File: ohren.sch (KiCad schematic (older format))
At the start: 33 parts, among them J1 Conn_01x19_MountingPin, U1 TLC5951RHA, U2 TLC5951RHA

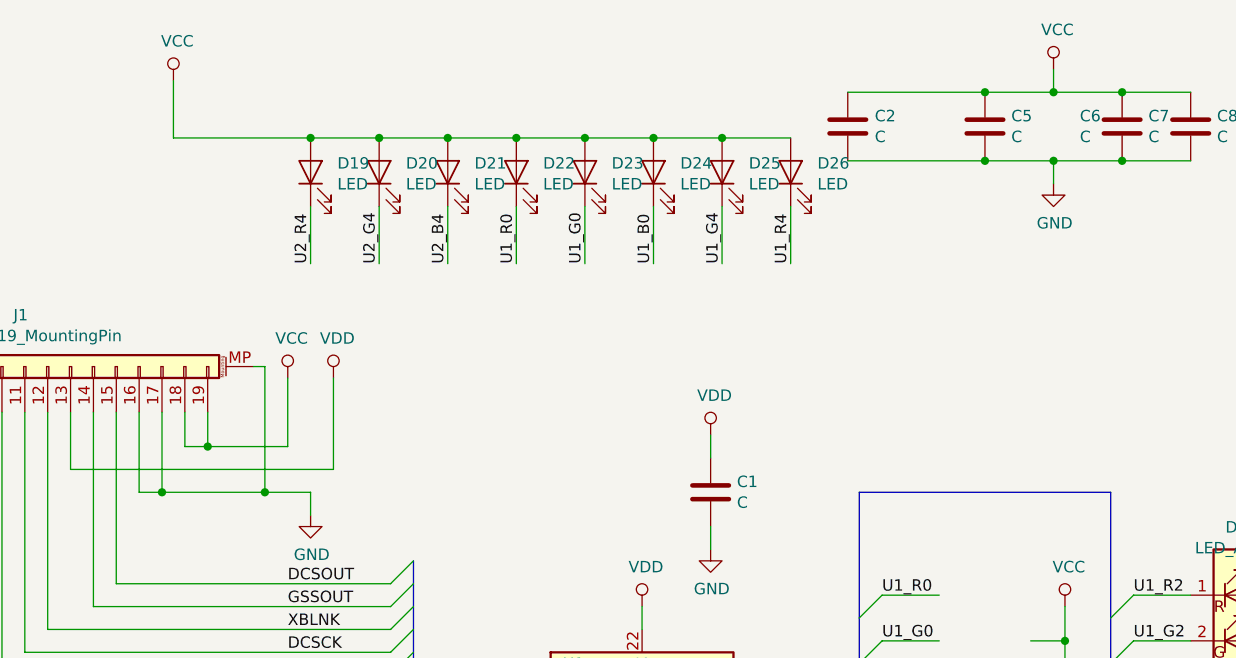
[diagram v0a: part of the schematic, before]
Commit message: Switch to more readily available Molex Easy-On 52746 series FFC
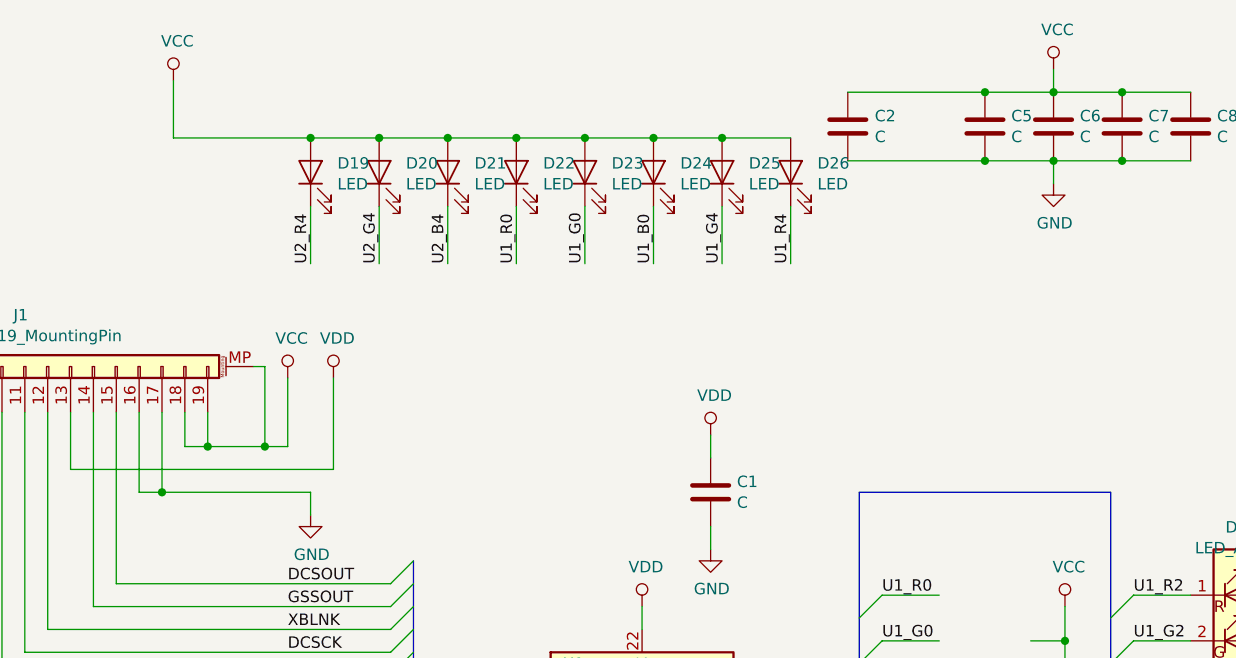
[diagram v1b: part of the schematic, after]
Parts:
- J1: footprint catear-pcb:Molex_Easy-On_54550-1971_1x19_P0.5mm_Horizontal -> catear-pcb:Molex_Easy-On_52746-1971_1x19_P0.5mm_Horizontal
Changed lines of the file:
@@
 Wire Wire Line
 	1900 2850 1900 2750
-Wire Wire Line
-	1900 2750 1700 2750
 Connection ~ 1250 2750
 Wire Wire Line
@@
 F 0 "J1" V 775 2118 50  0000 C CNN
 F 1 "Conn_01x19_MountingPin" V 684 2118 50  0000 C CNN
-F 2 "catear-pcb:Molex_Easy-On_54550-1971_1x19_P0.5mm_Horizontal" H 550 2200 50  0001 C CNN
+F 2 "catear-pcb:Molex_Easy-On_52746-1971_1x19_P0.5mm_Horizontal" H 550 2200 50  0001 C CNN
 F 3 "~" H 550 2200 50  0001 C CNN
 	1    550  2200
@@
 	750  3350 750  2400
 Wire Wire Line
-	1450 2550 1800 2550
+	1450 2550 1700 2550
 Wire Wire Line
 	1650 2200 1700 2200
-Wire Wire Line
-	1700 2200 1700 2750
-Connection ~ 1700 2750
-Wire Wire Line
-	1700 2750 1250 2750
 Wire Wire Line
 	4250 1000 4850 1000
@@
 $Comp
 L Device:C C6
-U 0 0 5D11A988
+U 1 1 5D11A988
 P 5150 1150
 F 0 "C6" H 5265 1196 50  0000 L CNN
@@
 F 2 "Capacitor_SMD:C_1210_3225Metric" H 5188 1000 50  0001 C CNN
 F 3 "~" H 5150 1150 50  0001 C CNN
-	0    5150 1150
+	1    5150 1150
 	1    0    0    -1
 $EndComp
+Wire Wire Line
+	1250 2750 1900 2750
+Wire Wire Line
+	1700 2200 1700 2550
 Wire Bus Line
 	5400 2750 5400 4550
@@
 Wire Bus Line
 	2350 3050 2350 6850
+Connection ~ 1700 2550
+Wire Wire Line
+	1700 2550 1800 2550
 $EndSCHEMATC

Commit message: Design revision D
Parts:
- removed C1: C, Capacitor_SMD:C_0805_2012Metric, symbol Device:C
- removed R1, R2: 2k4, Resistor_SMD:R_0402_1005Metric, symbol Device:R
- removed U1, U2: TLC5951RHA, Package_DFN_QFN:Texas_S-PVQFN-N40_EP4.15x4.15mm_ThermalVias, symbol ohren-rescue:TLC5951RHA-Driver_LED
- added U1: TLC5955RTQ, Package_DFN_QFN:QFN-56-1EP_8x8mm_P0.5mm_EP5.6x5.6mm_ThermalVias, symbol tlc5955:TLC5955RTQ
- C2, C5, C6, C7, C8: footprint Capacitor_SMD:C_1210_3225Metric -> Capacitor_SMD:C_0805_2012Metric
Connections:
- net labels added: GSCLK, LAT, SCLK, SIN, SOUT, U1_B10, U1_B11, U1_B12, U1_B13, U1_B14, U1_B15, U1_B8, U1_B9, U1_G10, U1_G11, U1_G12, U1_G13, U1_G14, U1_G15, U1_G8, U1_G9, U1_R10, U1_R11, U1_R12, U1_R13, U1_R14, U1_R15, U1_R8, U1_R9
- net labels removed: DCSCHAIN, DCSCK, DCSIN, DCSOUT, GSCKB, GSCKG, GSCKR, GSLAT, GSSCHAIN, GSSCK, GSSIN, GSSOUT, U2_B0, U2_B1, U2_B2, U2_B3, U2_B4, U2_B5, U2_B6, U2_B7, U2_G0, U2_G1, U2_G2, U2_G3, U2_G4, U2_G5, U2_G6, U2_G7, U2_R0, U2_R1, U2_R2, U2_R3, U2_R4, U2_R5, U2_R6, U2_R7, XBLNK
- wire segments 245 -> 212
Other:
- moved on the sheet: C2, C3, C5, C6, C7, C8, D10, D11, D12, D13, D14, D15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

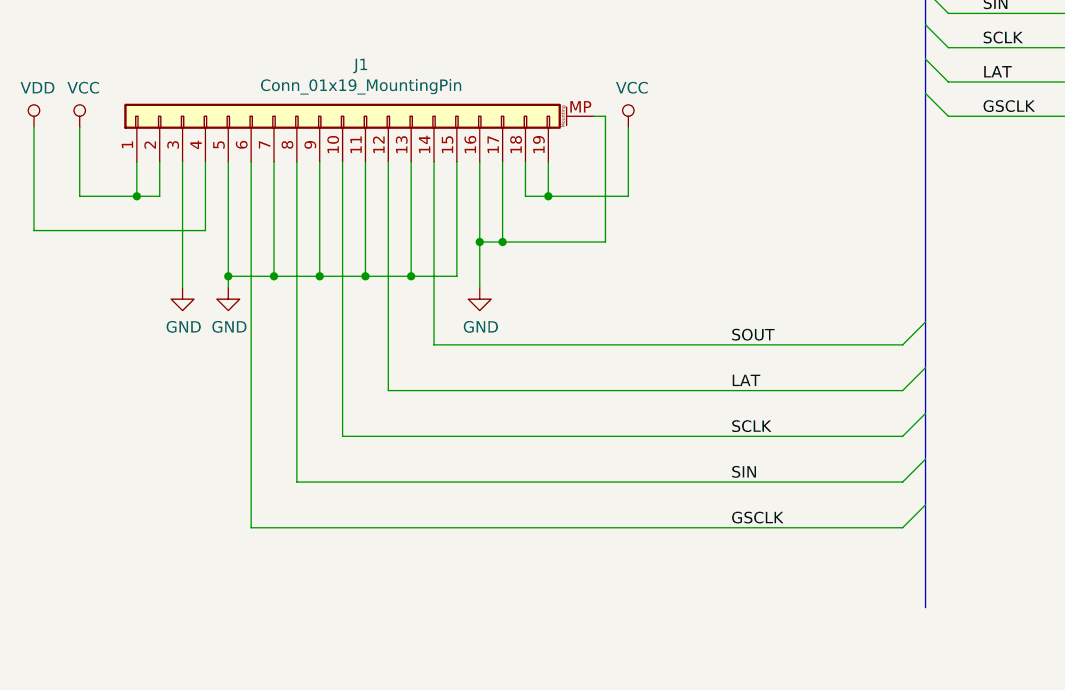
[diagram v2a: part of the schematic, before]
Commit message: Revise connector layout
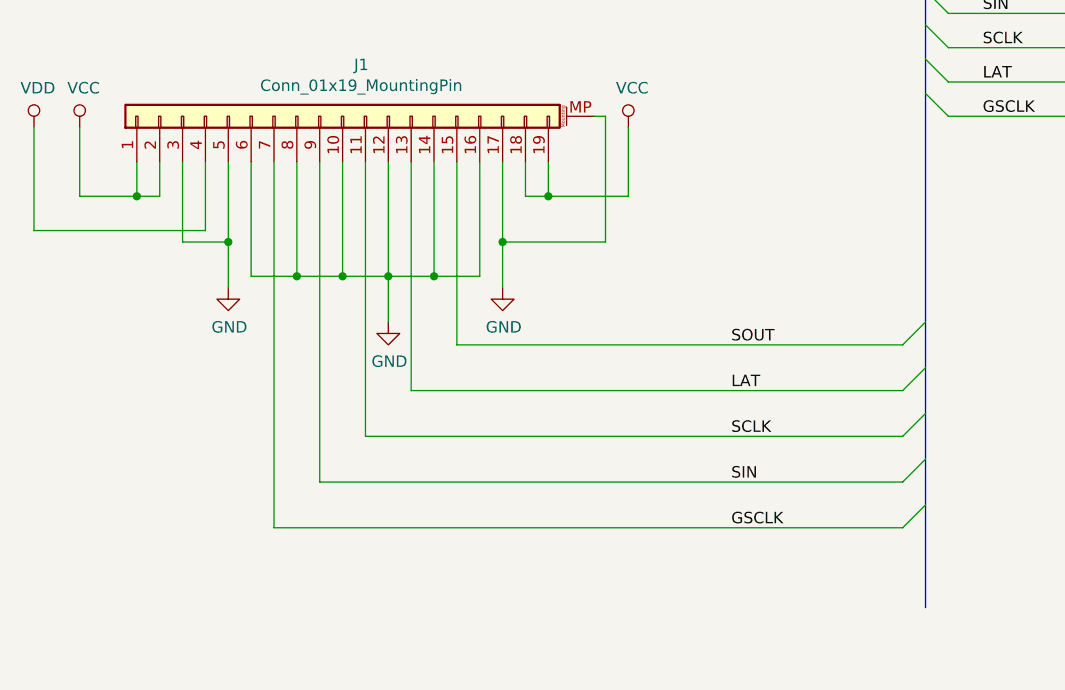
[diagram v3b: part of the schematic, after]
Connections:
- wire segments 212 -> 213
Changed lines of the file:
@@
 L power:GND #PWR0124
 U 1 1 5CDEC54B
-P 3100 3350
-F 0 "#PWR0124" H 3100 3100 50  0001 C CNN
-F 1 "GND" H 3105 3177 50  0000 C CNN
-F 2 "" H 3100 3350 50  0001 C CNN
-F 3 "" H 3100 3350 50  0001 C CNN
-	1    3100 3350
+P 3200 3350
+F 0 "#PWR0124" H 3200 3100 50  0001 C CNN
+F 1 "GND" H 3205 3177 50  0000 C CNN
+F 2 "" H 3200 3350 50  0001 C CNN
+F 3 "" H 3200 3350 50  0001 C CNN
+	1    3200 3350
 	1    0    0    -1
 $EndComp
@@
 	1    0    0    -1
 $EndComp
-Wire Wire Line
-	3100 2800 3100 3150
-Wire Wire Line
-	3100 3150 3200 3150
-$Comp
-L power:GND #PWR0109
-U 1 1 5CFE90D4
-P 1800 3350
-F 0 "#PWR0109" H 1800 3100 50  0001 C CNN
-F 1 "GND" H 1805 3177 50  0000 C CNN
-F 2 "" H 1800 3350 50  0001 C CNN
-F 3 "" H 1800 3350 50  0001 C CNN
-	1    1800 3350
-	1    0    0    -1
-$EndComp
-Wire Wire Line
-	3100 3350 3100 3150
-Connection ~ 3100 3150
 $Comp
 L power:GND #PWR0110
@@
 Wire Wire Line
 	1900 3100 1900 2800
-Wire Wire Line
-	3000 3300 3000 2800
-Wire Wire Line
-	1800 2800 1800 3350
-Wire Wire Line
-	2000 3300 2000 2800
-Wire Wire Line
-	2000 3350 2000 3300
-Connection ~ 2000 3300
-Wire Wire Line
-	2000 3300 2200 3300
-Wire Wire Line
-	2900 2800 2900 3600
-Wire Wire Line
-	2700 2800 2700 3800
-Wire Wire Line
-	2500 2800 2500 4000
-Wire Wire Line
-	2300 2800 2300 4200
-Wire Wire Line
-	2100 2800 2100 4400
-Wire Wire Line
-	2200 2800 2200 3300
-Connection ~ 2200 3300
-Wire Wire Line
-	2200 3300 2400 3300
-Wire Wire Line
-	2400 2800 2400 3300
-Connection ~ 2400 3300
-Wire Wire Line
-	2400 3300 2600 3300
-Wire Wire Line
-	2600 2800 2600 3300
-Connection ~ 2600 3300
-Wire Wire Line
-	2600 3300 2800 3300
-Wire Wire Line
-	2800 2800 2800 3300
-Connection ~ 2800 3300
-Wire Wire Line
-	2800 3300 3000 3300
 Entry Wire Line
 	4950 3600 5050 3500
-Wire Wire Line
-	2900 3600 4950 3600
 Entry Wire Line
 	4950 3800 5050 3700
@@
 Entry Wire Line
 	4950 4400 5050 4300
-Wire Wire Line
-	2100 4400 4950 4400
-Wire Wire Line
-	2300 4200 4950 4200
-Wire Wire Line
-	2500 4000 4950 4000
-Wire Wire Line
-	2700 3800 4950 3800
 Text Label 4200 4400 0    50   ~ 0
 GSCLK
@@
 Wire Wire Line
 	3650 3150 3200 3150
-Connection ~ 3200 3150
-$Comp
-L power:VCC #PWR?
+$Comp
+L power:VCC #PWR0105
 U 1 1 5D327796
 P 9050 2600
-F 0 "#PWR?" H 9050 2450 50  0001 C CNN
+F 0 "#PWR0105" H 9050 2450 50  0001 C CNN
 F 1 "VCC" H 9067 2773 50  0000 C CNN
 F 2 "" H 9050 2600 50  0001 C CNN
@@
 Connection ~ 9050 3000
 $Comp
-L power:VCC #PWR?
+L power:VCC #PWR0106
 U 1 1 5D33667A
 P 11200 2600
-F 0 "#PWR?" H 11200 2450 50  0001 C CNN
+F 0 "#PWR0106" H 11200 2450 50  0001 C CNN
 F 1 "VCC" H 11217 2773 50  0000 C CNN
 F 2 "" H 11200 2600 50  0001 C CNN
@@
 Connection ~ 11200 7250
 $Comp
-L power:VCC #PWR?
+L power:VCC #PWR0107
 U 1 1 5D344968
 P 11200 6850
-F 0 "#PWR?" H 11200 6700 50  0001 C CNN
+F 0 "#PWR0107" H 11200 6700 50  0001 C CNN
 F 1 "VCC" H 11217 7023 50  0000 C CNN
 F 2 "" H 11200 6850 50  0001 C CNN
@@
 	11200 6850 11200 7250
 $Comp
-L power:VCC #PWR?
+L power:VCC #PWR0108
 U 1 1 5D352929
 P 9050 6850
-F 0 "#PWR?" H 9050 6700 50  0001 C CNN
+F 0 "#PWR0108" H 9050 6700 50  0001 C CNN
 F 1 "VCC" H 9067 7023 50  0000 C CNN
 F 2 "" H 9050 6850 50  0001 C CNN
@@
 Wire Wire Line
 	9050 6850 9050 7250
+Connection ~ 9050 7250
+Wire Wire Line
+	2100 2800 2100 3300
+Wire Wire Line
+	3000 2800 3000 3600
+Wire Wire Line
+	3000 3600 4950 3600
+Wire Wire Line
+	2800 2800 2800 3800
+Wire Wire Line
+	2800 3800 4950 3800
+Wire Wire Line
+	2600 2800 2600 4000
+Wire Wire Line
+	2600 4000 4950 4000
+Wire Wire Line
+	2400 2800 2400 4200
+Wire Wire Line
+	2400 4200 4950 4200
+Wire Wire Line
+	2200 2800 2200 4400
+Wire Wire Line
+	2200 4400 4950 4400
+Wire Wire Line
+	2300 2800 2300 3300
+Wire Wire Line
+	2300 3300 2500 3300
+Wire Wire Line
+	2500 3300 2500 2800
+Connection ~ 2500 3300
+Wire Wire Line
+	2900 2800 2900 3300
+Wire Wire Line
+	2700 2800 2700 3300
+Wire Wire Line
+	2500 3300 2700 3300
+Connection ~ 2700 3300
+Wire Wire Line
+	2700 3300 2900 3300
+Wire Wire Line
+	2000 2800 2000 3150
+Wire Wire Line
+	2100 3300 2300 3300
+Connection ~ 2300 3300
+Wire Wire Line
+	1800 2800 1800 3150
+Wire Wire Line
+	1800 3150 2000 3150
+Connection ~ 2000 3150
+Wire Wire Line
+	2000 3150 2000 3350
+Wire Wire Line
+	3100 2800 3100 3300
+Wire Wire Line
+	3100 3300 2900 3300
+Connection ~ 2900 3300
+Wire Wire Line
+	3200 3350 3200 3150
+Connection ~ 3200 3150
+$Comp
+L power:GND #PWR?
+U 1 1 5D48D865
+P 2700 3500
+F 0 "#PWR?" H 2700 3250 50  0001 C CNN
+F 1 "GND" H 2705 3327 50  0000 C CNN
+F 2 "" H 2700 3500 50  0001 C CNN
+F 3 "" H 2700 3500 50  0001 C CNN
+	1    2700 3500
+	1    0    0    -1
+$EndComp
+Wire Wire Line
+	2700 3500 2700 3300
 Wire Bus Line
 	5050 1250 5050 4750
@@
 Wire Bus Line
 	7600 6700 7600 10650
-Connection ~ 9050 7250
 $EndSCHEMATC

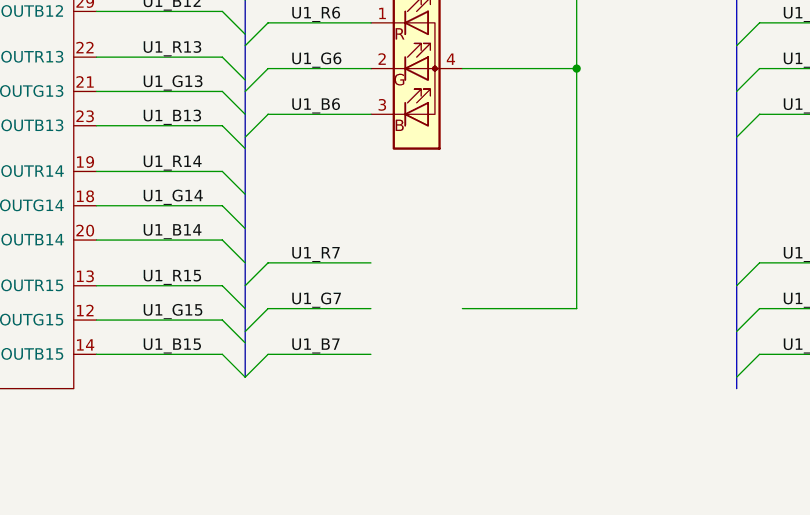
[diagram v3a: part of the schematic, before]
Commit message: Add TP to unused TLC pin
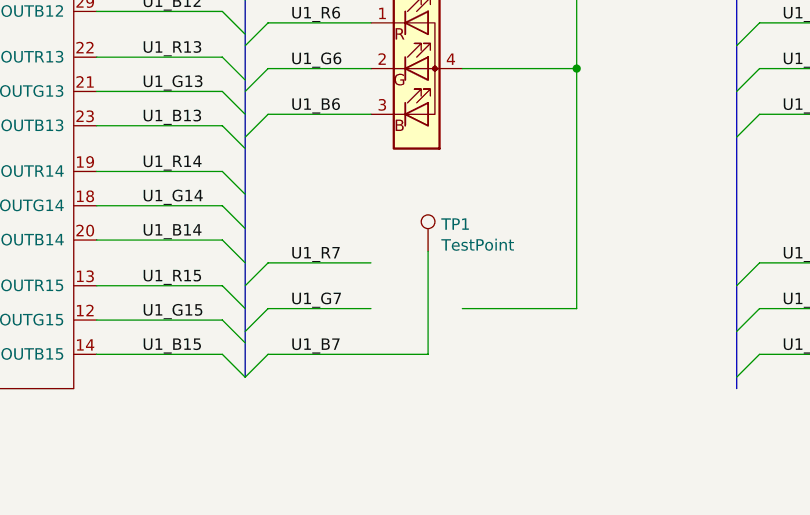
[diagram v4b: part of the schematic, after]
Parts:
- added TP1: TestPoint, catear-pcb:TestPoint_0.5x1mm, symbol Connector:TestPoint
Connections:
- wire segments 213 -> 214
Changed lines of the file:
@@
 U1_R7
-Wire Wire Line
-	8150 10550 7700 10550
 Wire Wire Line
 	8150 10350 7700 10350
@@
 Connection ~ 3200 3150
 $Comp
-L power:GND #PWR?
+L power:GND #PWR0109
 U 1 1 5D48D865
 P 2700 3500
-F 0 "#PWR?" H 2700 3250 50  0001 C CNN
+F 0 "#PWR0109" H 2700 3250 50  0001 C CNN
 F 1 "GND" H 2705 3327 50  0000 C CNN
 F 2 "" H 2700 3500 50  0001 C CNN
@@
 Wire Wire Line
 	2700 3500 2700 3300
+$Comp
+L Connector:TestPoint TP1
+U 1 1 5CCD2D62
+P 8400 10100
+F 0 "TP1" H 8458 10218 50  0000 L CNN
+F 1 "TestPoint" H 8458 10127 50  0000 L CNN
+F 2 "catear-pcb:TestPoint_0.5x1mm" H 8600 10100 50  0001 C CNN
+F 3 "~" H 8600 10100 50  0001 C CNN
+	1    8400 10100
+	1    0    0    -1
+$EndComp
+Wire Wire Line
+	8400 10100 8400 10550
+Wire Wire Line
+	7700 10550 8400 10550
 Wire Bus Line
 	5050 1250 5050 4750
